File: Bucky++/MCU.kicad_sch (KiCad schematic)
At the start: 39 parts, among them J15 502585-0470, J16 FTSH-105-01-F-D-RA-K, J1702 505110-3091, J1801 S2B-PH-SM4-TB, J403 USB4105-GF-A, Q1401 PMV90ENER, U1801 DGD0216WT-7, U401 STM32G483RET6, Y201 ABM8W-48.0000MHZ-4-D1X-T3

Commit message: created Bucky++ with new template and e-fuses
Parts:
- removed R401: 33k 1% 1/16W, 0_resistor_smd:R_0402_1005_DensityHigh, symbol Device:R
- removed unit 2 of U401
- added U1: STM32G483RET6, Package_QFP:LQFP-64_10x10mm_P0.5mm, symbol MCU_ST_STM32G4:STM32G483RETx
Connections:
- net +3.3VA: now also U1.28 (VREF+), U1.29 (VDDA)
- net +3V3: now also U1.1 (VBAT), U1.16 (VDD), U1.32 (VDD), U1.48 (VDD), U1.64 (VDD)
- net GND: now also U1.15 (VSS), U1.27 (VSSA), U1.31 (VSS), U1.47 (VSS), U1.63 (VSS)
- net PRE_EN: no longer names the net of U401.24 (PB0)
- net PRE_FLT: no longer names the net of U401.23 (PC5)
- no-connect marks 38 -> 40
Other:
- company: (none) -> ${COMPANY}
- title: (none) -> MCU
- moved on the sheet: C1709, C1801, C1802, C203, C207, C403, C404, C406, C407, C408, C409, C410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

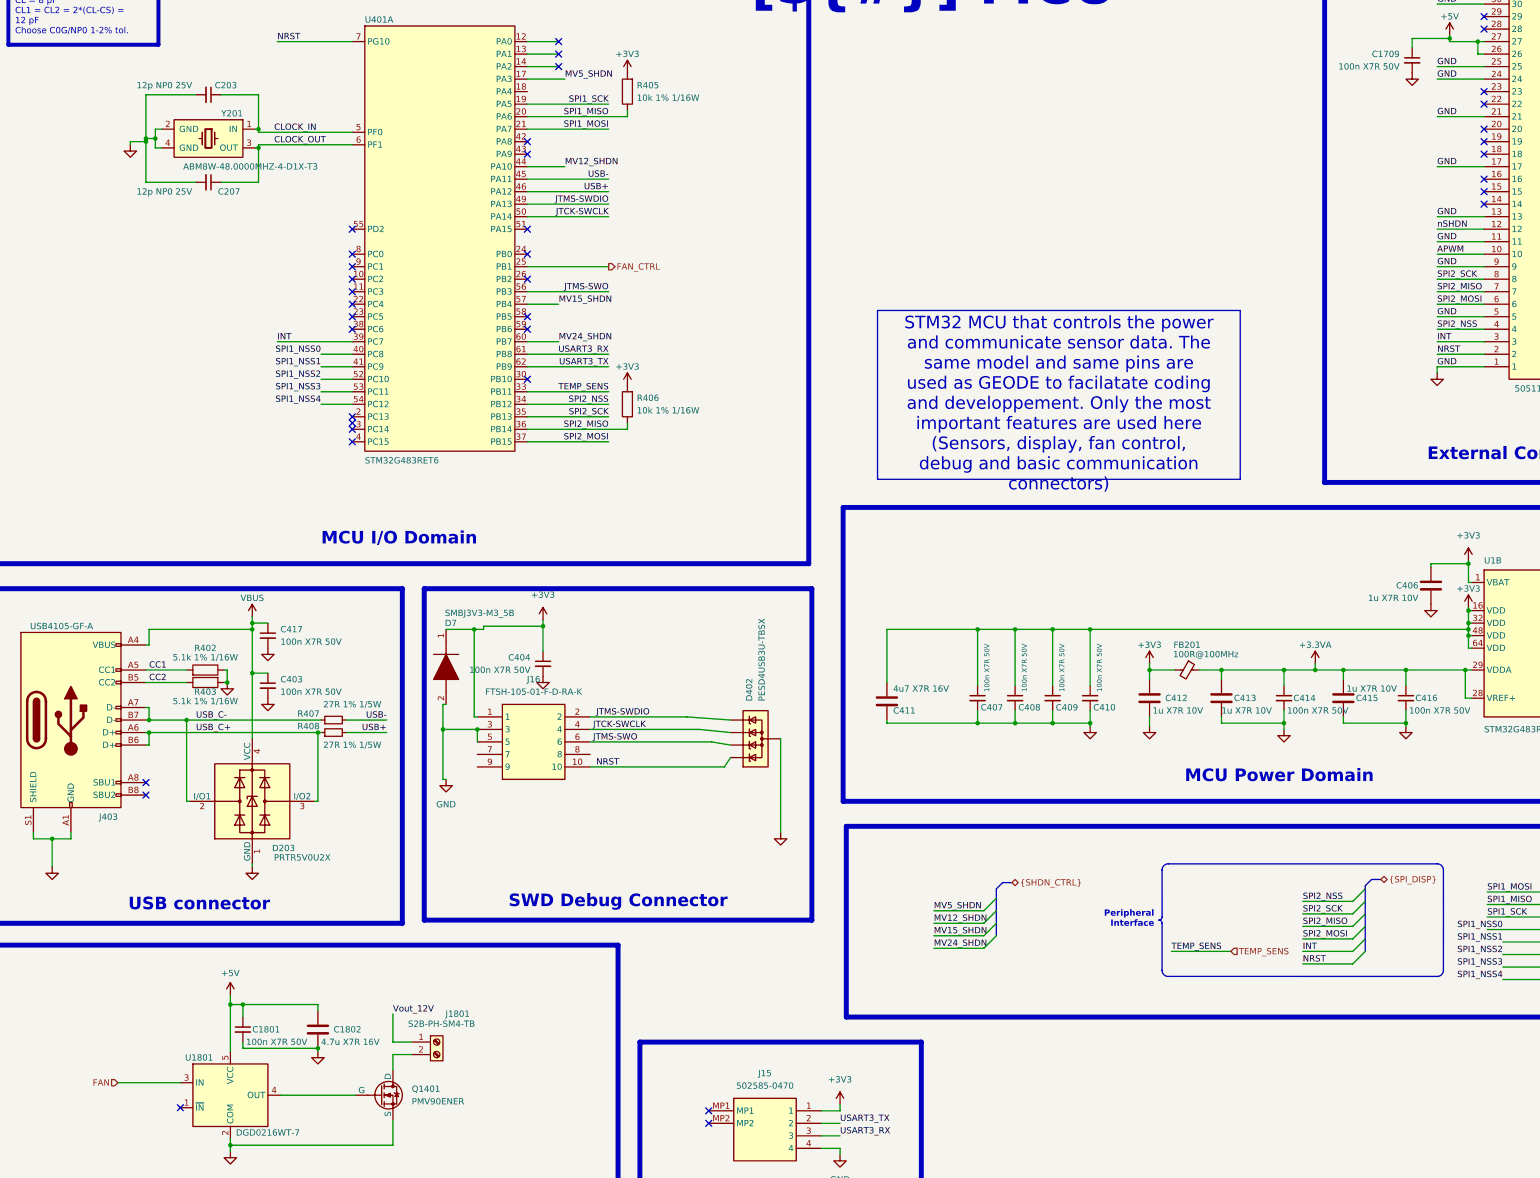
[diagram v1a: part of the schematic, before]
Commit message: added over-current protection on main input
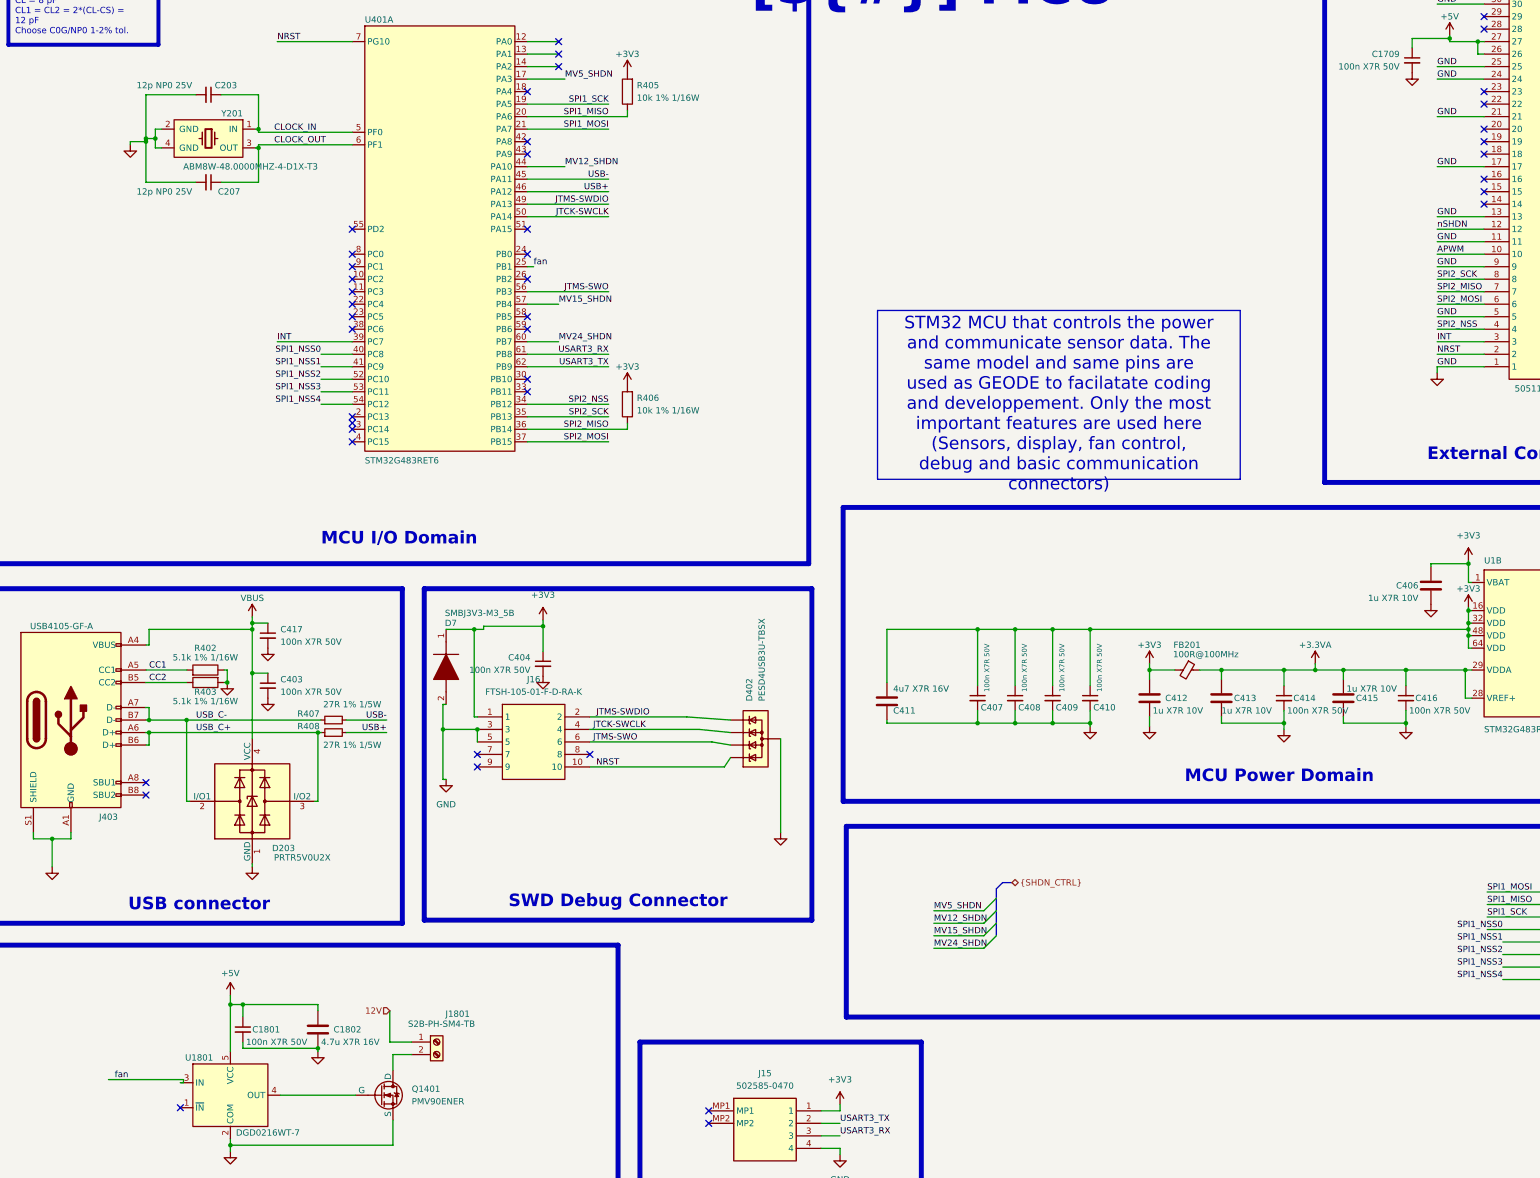
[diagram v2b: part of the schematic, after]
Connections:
- net FAN_CTRL is gone; now on net fan: U401.25 (PB1)
- net FAN renamed fan
- net TEMP_SENS: no longer names the net of U401.33 (PB11)
- net Vout_12V renamed 12V
- no-connect marks 40 -> 45

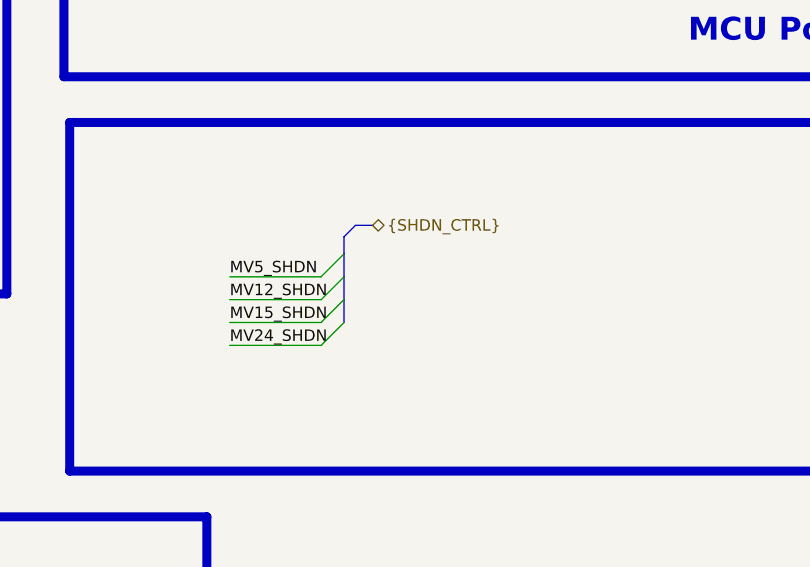
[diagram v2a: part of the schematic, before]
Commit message: fixed errors and added protection diodes
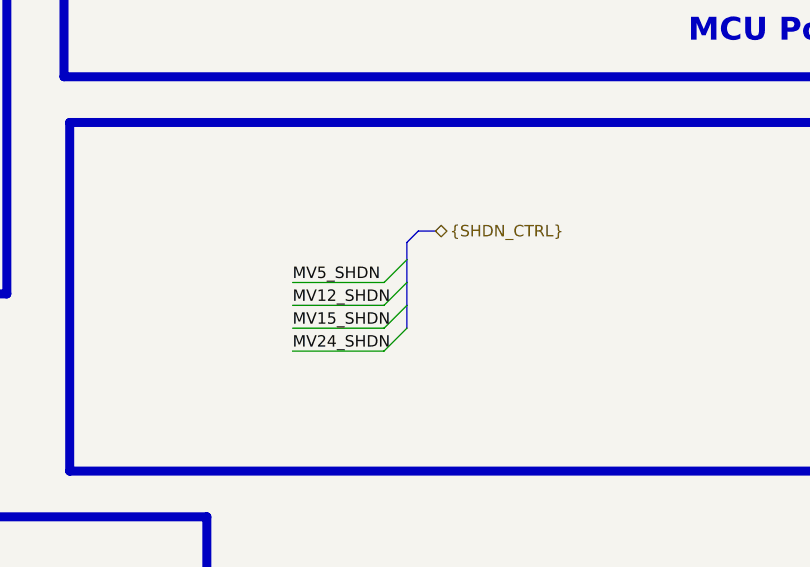
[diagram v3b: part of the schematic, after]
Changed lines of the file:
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@@
 	)
 	(bus_entry
-		(at 222.25 214.63)
+		(at 229.235 215.265)
 		(size -2.54 2.54)
 		(stroke
@@
 	)
 	(bus_entry
-		(at 222.25 219.71)
+		(at 229.235 220.345)
 		(size -2.54 2.54)
 		(stroke
@@
 	)
 	(bus_entry
-		(at 222.25 217.17)
+		(at 229.235 217.805)
 		(size -2.54 2.54)
 		(stroke
@@
 	)
 	(bus_entry
-		(at 222.25 212.09)
+		(at 229.235 212.725)
 		(size -2.54 2.54)
 		(stroke
@@
 	(wire
 		(pts
-			(xy 209.55 222.25) (xy 219.71 222.25)
+			(xy 216.535 222.885) (xy 226.695 222.885)
 		)
 		(stroke
@@
 	(wire
 		(pts
-			(xy 209.55 217.17) (xy 219.71 217.17)
+			(xy 216.535 217.805) (xy 226.695 217.805)
 		)
 		(stroke
@@
 	(bus
 		(pts
-			(xy 223.52 208.915) (xy 222.25 210.185)
+			(xy 230.505 209.55) (xy 229.235 210.82)
 		)
 		(stroke
@@
 	(bus
 		(pts
-			(xy 222.25 217.17) (xy 222.25 219.71)
+			(xy 229.235 217.805) (xy 229.235 220.345)
 		)
 		(stroke
@@
 	(bus
 		(pts
-			(xy 222.25 214.63) (xy 222.25 217.17)
+			(xy 229.235 215.265) (xy 229.235 217.805)
 		)
 		(stroke
@@
 	(wire
 		(pts
-			(xy 209.55 219.71) (xy 219.71 219.71)
+			(xy 216.535 220.345) (xy 226.695 220.345)
 		)
 		(stroke
@@
 	(bus
 		(pts
-			(xy 225.425 208.915) (xy 223.52 208.915)
+			(xy 232.41 209.55) (xy 230.505 209.55)
 		)
 		(stroke
@@
 	(bus
 		(pts
-			(xy 222.25 212.09) (xy 222.25 214.63)
+			(xy 229.235 212.725) (xy 229.235 215.265)
 		)
 		(stroke
@@
 	(wire
 		(pts
-			(xy 209.55 214.63) (xy 219.71 214.63)
+			(xy 216.535 215.265) (xy 226.695 215.265)
 		)
 		(stroke
@@
 	(bus
 		(pts
-			(xy 222.25 210.185) (xy 222.25 212.09)
+			(xy 229.235 210.82) (xy 229.235 212.725)
 		)
 		(stroke
@@
 	)
 	(label "MV24_SHDN"
-		(at 209.55 222.25 0)
+		(at 216.535 222.885 0)
 		(effects
 			(font
@@
 	)
 	(label "MV15_SHDN"
-		(at 209.55 219.71 0)
+		(at 216.535 220.345 0)
 		(effects
 			(font
@@
 	)
 	(label "MV12_SHDN"
-		(at 209.55 217.17 0)
+		(at 216.535 217.805 0)
 		(effects
 			(font
@@
 	)
 	(label "MV5_SHDN"
-		(at 209.55 214.63 0)
+		(at 216.535 215.265 0)
 		(effects
 			(font
@@
 	(hierarchical_label "{SHDN_CTRL}"
 		(shape bidirectional)
-		(at 225.425 208.915 0)
+		(at 232.41 209.55 0)
 		(effects
 			(font

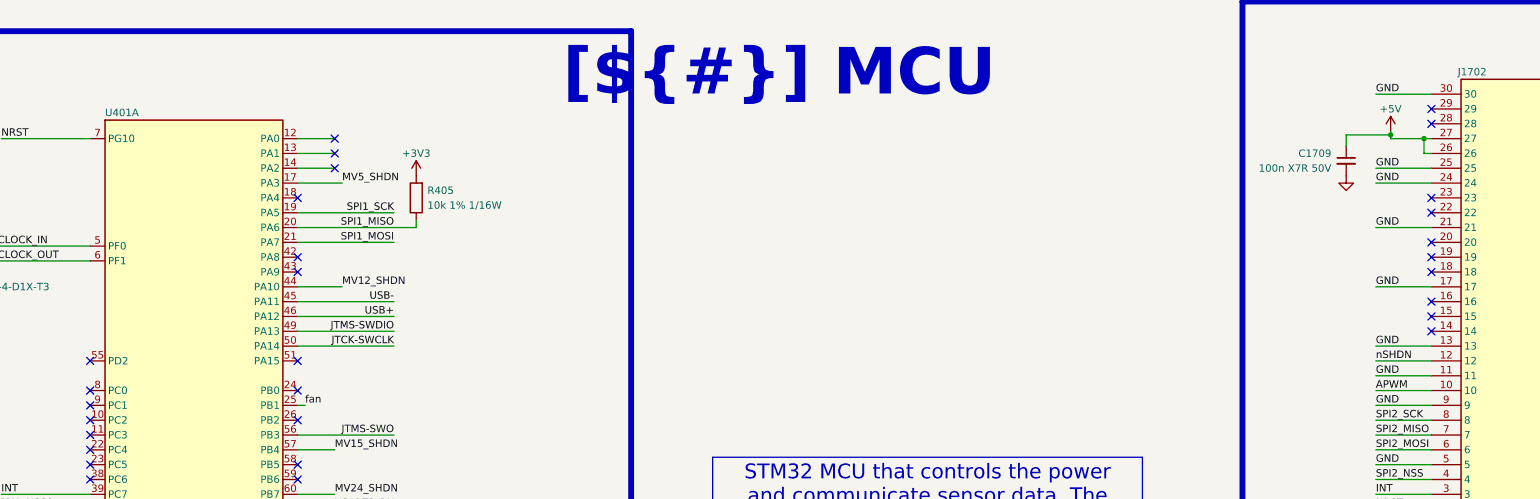
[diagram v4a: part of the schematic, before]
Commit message: initial component placement
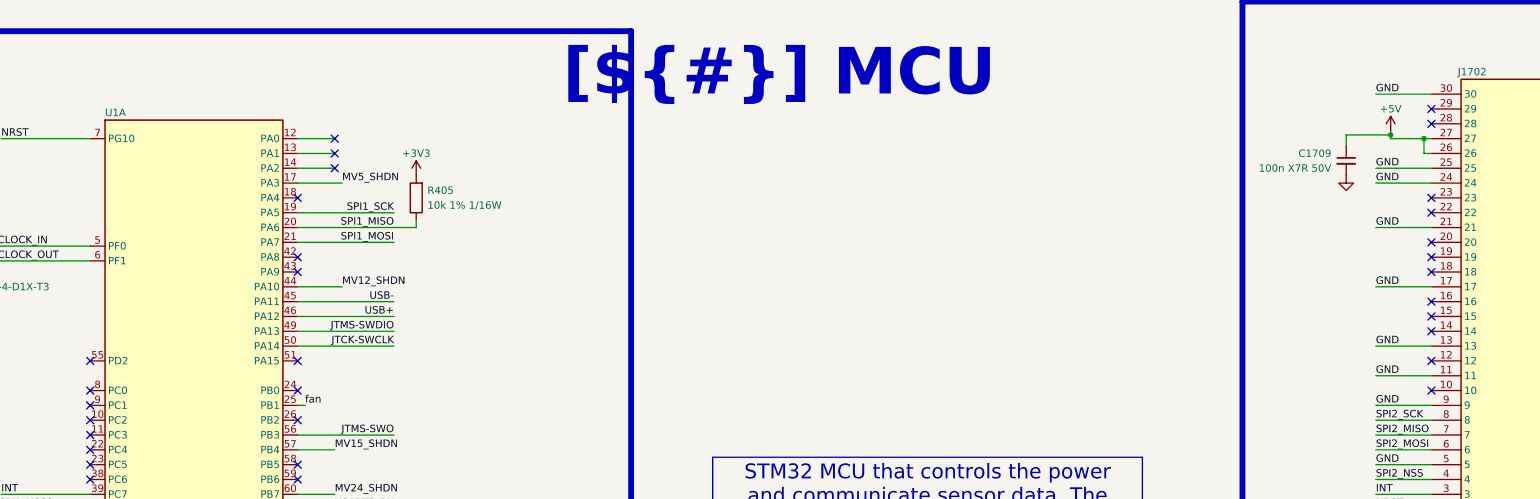
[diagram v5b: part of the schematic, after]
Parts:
- renumbered U401 to U1
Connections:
- net APWM: no longer names the net of J1702.10
- net nSHDN: no longer names the net of J1702.12
- no-connect marks 45 -> 47
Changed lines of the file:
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@@
 	)
 	(no_connect
+		(at 321.31 76.2)
+	)
+	(no_connect
 		(at 321.31 58.42)
 	)
@@
 	)
 	(no_connect
+		(at 321.31 81.28)
+	)
+	(no_connect
 		(at 127 48.26)
 	)
@@
 	(wire
 		(pts
-			(xy 311.785 81.28) (xy 321.31 81.28)
-		)
-		(stroke
-			(width 0)
-			(type default)
-		)
-	)
-	(wire
-		(pts
 			(xy 26.67 200.025) (xy 30.48 200.025)
 		)
@@
 	(wire
 		(pts
-			(xy 311.785 76.2) (xy 321.31 76.2)
-		)
-		(stroke
-			(width 0)
-			(type default)
-		)
-	)
-	(wire
-		(pts
 			(xy 310.515 144.145) (xy 310.515 144.78)
 		)
@@
 		)
 	)
-	(label "APWM"
-		(at 311.785 81.28 0)
-		(effects
-			(font
-				(size 1.27 1.27)
-			)
-			(justify left bottom)
-		)
-	)
 	(label "MV24_SHDN"
 		(at 216.535 222.885 0)
@@
 		)
 	)
-	(label "nSHDN"
-		(at 311.785 76.2 0)
-		(effects
-			(font
-				(size 1.27 1.27)
-			)
-			(justify left bottom)
-		)
-	)
 	(label "SPI1_NSS0"
 		(at 85.09 101.6 180)
@@
 		(on_board yes)
 		(dnp no)
-		(property "Reference" "U401"
+		(property "Reference" "U1"
 			(at 93.98 33.655 0)
 			(effects
@@
 			(project "Bucky++"
 				(path "/0650c7a8-acba-429c-9f8e-eec0baf0bc1c/fede4c36-00cc-4d3d-b71c-5243ba232202/694c70cd-5237-46a2-a5ef-62c4b649ef6f"
-					(reference "U401")
+					(reference "U1")
 					(unit 1)
 				)
